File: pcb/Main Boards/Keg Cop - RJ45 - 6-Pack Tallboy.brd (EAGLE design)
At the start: 65 x 51 mm, 17 parts, among them X1 RJ45-8X, X2 RJ45-8X

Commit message: Swap pins, split dirs
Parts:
- moved RELAY 0.40 mm to (13.5, 47.5)
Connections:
- net COOL: now also D32.IO4, RELAY.3; no longer D32.IO0, RELAY.2
- net KDAT: now also D32.IO14; no longer D32.IO27
- net KEG1: now also D32.IO0; no longer D32.IO4
- net SOL: now also D32.IO27, RELAY.2; no longer D32.IO14, RELAY.3
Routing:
- net COOL: track 72.7 -> 91.1 mm
- net KEG1: track 14.9 -> 11.2 mm
- net KDAT: track 25.2 -> 26.1 mm
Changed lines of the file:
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@@
 <wire x1="0" y1="50" x2="0" y2="1" width="0" layer="20"/>
 <wire x1="0" y1="1" x2="1" y2="0" width="0" layer="20" curve="90"/>
-<text x="9.7" y="45.3" size="0.8128" layer="25" align="top-center">G</text>
-<text x="12.3" y="45.3" size="0.8128" layer="25" align="top-center">C</text>
-<text x="14.8" y="45.3" size="0.8128" layer="25" align="top-center">S</text>
-<text x="17.4" y="45.3" size="0.8128" layer="25" align="top-center">V</text>
+<text x="9.7" y="45.7" size="0.8128" layer="25" align="top-center">G</text>
+<text x="14.8" y="45.7" size="0.8128" layer="25" align="top-center">C</text>
+<text x="12.3" y="45.7" size="0.8128" layer="25" align="top-center">S</text>
+<text x="17.4" y="45.7" size="0.8128" layer="25" align="top-center">V</text>
 <text x="9.7" y="39.4" size="0.8128" layer="25" align="top-center">G</text>
 <text x="12.2" y="39.4" size="0.8128" layer="25" align="top-center">V</text>
@@
 <elements>
 <element name="D32" library="Donnie" package="D32_NO_BATT" value="Lolin D32" x="32.5" y="29.27" smashed="yes"/>
-<element name="RELAY" library="Donnie" package="MA04-1" package3d_urn="urn:adsk.eagle:package:8337/1" value="4-PIN" x="13.517" y="47.059975" smashed="yes">
-<attribute name="MF" value="" x="13.517" y="47.059975" size="1.778" layer="27" display="off"/>
-<attribute name="MPN" value="" x="13.517" y="47.059975" size="1.778" layer="27" display="off"/>
-<attribute name="NAME" x="8.437" y="48.710975" size="0.8128" layer="25"/>
-<attribute name="OC_FARNELL" value="unknown" x="13.517" y="47.059975" size="1.778" layer="27" display="off"/>
-<attribute name="OC_NEWARK" value="unknown" x="13.517" y="47.059975" size="1.778" layer="27" display="off"/>
-<attribute name="POPULARITY" value="41" x="13.517" y="47.059975" size="1.778" layer="27" display="off"/>
+<element name="RELAY" library="Donnie" package="MA04-1" package3d_urn="urn:adsk.eagle:package:8337/1" value="4-PIN" x="13.517" y="47.459975" smashed="yes">
+<attribute name="MF" value="" x="13.517" y="47.459975" size="1.778" layer="27" display="off"/>
+<attribute name="MPN" value="" x="13.517" y="47.459975" size="1.778" layer="27" display="off"/>
+<attribute name="NAME" x="8.437" y="49.110975" size="0.8128" layer="25"/>
+<attribute name="OC_FARNELL" value="unknown" x="13.517" y="47.459975" size="1.778" layer="27" display="off"/>
+<attribute name="OC_NEWARK" value="unknown" x="13.517" y="47.459975" size="1.778" layer="27" display="off"/>
+<attribute name="POPULARITY" value="41" x="13.517" y="47.459975" size="1.778" layer="27" display="off"/>
 </element>
 <element name="R1" library="SparkFun-Resistors" library_urn="urn:adsk.eagle:library:532" package="AXIAL-0.3" package3d_urn="urn:adsk.eagle:package:39658/1" value="2.2kΩ" x="28.55335" y="36.8892" smashed="yes" rot="R180">
@@
 <contactref element="C2" pad="1"/>
 <wire x1="22.61" y1="49.59" x2="21.07" y2="49.59" width="1.016" layer="1"/>
-<wire x1="17.327" y1="47.059975" x2="17.327" y2="48.927" width="1.016" layer="1"/>
-<wire x1="17.327" y1="48.927" x2="18" y2="49.6" width="1.016" layer="1"/>
-<wire x1="18" y1="49.6" x2="21.16585" y2="49.6" width="1.016" layer="1"/>
+<wire x1="17.327" y1="47.459975" x2="17.327" y2="49.127" width="1.016" layer="1"/>
+<wire x1="17.327" y1="49.127" x2="17.8" y2="49.6" width="1.016" layer="1"/>
+<wire x1="17.8" y1="49.6" x2="21.16585" y2="49.6" width="1.016" layer="1"/>
 <wire x1="21.16585" y1="49.6" x2="21.07" y2="49.59" width="1.016" layer="1"/>
 <wire x1="32.36335" y1="26.7322" x2="32.36335" y2="29.27145" width="1.016" layer="1"/>
@@
 <contactref element="C3" pad="2"/>
 <contactref element="X1" pad="7"/>
-<wire x1="9.707" y1="41.2" x2="9.707" y2="47.059975" width="1.016" layer="1"/>
+<wire x1="9.707" y1="41.2" x2="9.707" y2="47.459975" width="1.016" layer="1"/>
 <wire x1="35.15785" y1="45.698" x2="35.15785" y2="48.497" width="1.016" layer="1"/>
 <wire x1="35.15785" y1="48.497" x2="35.16285" y2="48.502" width="1.016" layer="1"/>
@@
 </signal>
 <signal name="SOL">
-<contactref element="RELAY" pad="3"/>
-<contactref element="D32" pad="IO14"/>
-<wire x1="21.07" y1="24.19" x2="19.31" y2="24.19" width="1.016" layer="16"/>
-<wire x1="18.7" y1="40.6" x2="14.787" y2="44.513" width="1.016" layer="16"/>
-<wire x1="14.787" y1="44.513" x2="14.787" y2="47.059975" width="1.016" layer="16"/>
-<wire x1="19.31" y1="24.19" x2="18.7" y2="24.8" width="1.016" layer="16"/>
-<wire x1="18.7" y1="24.8" x2="18.7" y2="40.6" width="1.016" layer="16"/>
+<contactref element="RELAY" pad="2"/>
+<wire x1="14.2" y1="45.1" x2="18.7" y2="40.6" width="1.016" layer="16"/>
+<wire x1="14.2" y1="45.1" x2="12.8" y2="45.1" width="1.016" layer="16"/>
+<wire x1="12.8" y1="45.1" x2="12.247" y2="45.653" width="1.016" layer="16"/>
+<wire x1="12.247" y1="45.653" x2="12.247" y2="47.459975" width="1.016" layer="16"/>
+<contactref element="D32" pad="IO27"/>
+<wire x1="18.7" y1="40.6" x2="18.7" y2="27.6" width="1.016" layer="16"/>
+<wire x1="18.7" y1="27.6" x2="19.57" y2="26.73" width="1.016" layer="16"/>
+<wire x1="19.57" y1="26.73" x2="21.07" y2="26.73" width="1.016" layer="16"/>
 </signal>
 <signal name="COOL">
-<contactref element="RELAY" pad="2"/>
-<contactref element="D32" pad="IO0"/>
-<wire x1="25.41" y1="19.11" x2="43.93" y2="19.11" width="1.016" layer="16"/>
 <wire x1="23.2" y1="10.2" x2="22.6" y2="9.6" width="1.016" layer="16"/>
 <wire x1="22.6" y1="9.6" x2="19.6" y2="9.6" width="1.016" layer="16"/>
 <wire x1="18.75555625" y1="10.44444375" x2="19.6" y2="9.6" width="1.016" layer="16"/>
-<wire x1="12.247" y1="47.059975" x2="12.247" y2="45.053" width="1.016" layer="16"/>
 <wire x1="15.6" y1="21.6" x2="18.75555625" y2="18.44444375" width="1.016" layer="16"/>
 <wire x1="18.75555625" y1="18.44444375" x2="18.75555625" y2="10.44444375" width="1.016" layer="16"/>
-<wire x1="12.247" y1="45.053" x2="15.6" y2="41.7" width="1.016" layer="16"/>
-<wire x1="15.6" y1="41.7" x2="15.6" y2="21.6" width="1.016" layer="16"/>
+<wire x1="15.6" y1="21.6" x2="15.6" y2="41.7" width="1.016" layer="16"/>
 <wire x1="23.2" y1="10.2" x2="23.2" y2="16.9" width="1.016" layer="16"/>
 <wire x1="23.2" y1="16.9" x2="25.41" y2="19.11" width="1.016" layer="16"/>
+<contactref element="RELAY" pad="3"/>
+<wire x1="15.6" y1="41.7" x2="13.6" y2="43.7" width="1.016" layer="16"/>
+<wire x1="8.2" y1="43.7" x2="6.8" y2="45.1" width="1.016" layer="16"/>
+<wire x1="6.8" y1="45.1" x2="6.8" y2="48.3" width="1.016" layer="16"/>
+<wire x1="14.787" y1="49.213" x2="14.787" y2="47.459975" width="1.016" layer="16"/>
+<wire x1="13.6" y1="43.7" x2="8.2" y2="43.7" width="1.016" layer="16"/>
+<wire x1="6.8" y1="48.3" x2="8.4" y2="49.9" width="1.016" layer="16"/>
+<wire x1="8.4" y1="49.9" x2="14.1" y2="49.9" width="1.016" layer="16"/>
+<wire x1="14.1" y1="49.9" x2="14.787" y2="49.213" width="1.016" layer="16"/>
+<contactref element="D32" pad="IO4"/>
+<wire x1="25.41" y1="19.11" x2="27.95" y2="21.65" width="1.016" layer="16"/>
+<wire x1="27.95" y1="21.65" x2="43.93" y2="21.65" width="1.016" layer="16"/>
 </signal>
 <signal name="RDAT">
@@
 <signal name="KDAT">
 <contactref element="R5" pad="P$2"/>
-<contactref element="D32" pad="IO27"/>
 <contactref element="X1" pad="5"/>
 <contactref element="X1" pad="6"/>
@@
 <wire x1="10.635" y1="13.12" x2="11.905" y2="14.39" width="1.016" layer="1"/>
 <wire x1="11.905" y1="14.39" x2="11.905" y2="21.505" width="1.016" layer="1"/>
-<wire x1="17.13" y1="26.73" x2="21.07" y2="26.73" width="1.016" layer="1"/>
-<wire x1="11.905" y1="21.505" x2="17.13" y2="26.73" width="1.016" layer="1"/>
-<wire x1="24.74335" y1="26.7322" x2="21.17805" y2="26.7322" width="1.016" layer="1"/>
-<wire x1="21.17805" y1="26.7322" x2="21.07" y2="26.73" width="1.016" layer="1"/>
+<contactref element="D32" pad="IO14"/>
+<wire x1="11.905" y1="21.505" x2="14.59" y2="24.19" width="1.016" layer="1"/>
+<wire x1="14.59" y1="24.19" x2="21.07" y2="24.19" width="1.016" layer="1"/>
+<wire x1="21.07" y1="24.19" x2="23.69" y2="24.19" width="1.016" layer="1"/>
+<wire x1="24.74335" y1="25.24335" x2="24.74335" y2="26.7322" width="1.016" layer="1"/>
+<wire x1="23.69" y1="24.19" x2="24.74335" y2="25.24335" width="1.016" layer="1"/>
 </signal>
 <signal name="KEG4">
@@
 </signal>
 <signal name="KEG1">
-<contactref element="D32" pad="IO4"/>
 <contactref element="X2" pad="1"/>
-<wire x1="49.2" y1="20.4" x2="47.95" y2="21.65" width="1.016" layer="1"/>
-<wire x1="47.95" y1="21.65" x2="43.93" y2="21.65" width="1.016" layer="1"/>
 <wire x1="50.555" y1="11.85" x2="49.2" y2="13.205" width="1.016" layer="1"/>
-<wire x1="49.2" y1="13.205" x2="49.2" y2="20.4" width="1.016" layer="1"/>
+<contactref element="D32" pad="IO0"/>
+<wire x1="49.2" y1="13.205" x2="47.3" y2="15.105" width="1.016" layer="1"/>
+<wire x1="47.3" y1="15.105" x2="47.3" y2="17.8" width="1.016" layer="1"/>
+<wire x1="45.99" y1="19.11" x2="43.93" y2="19.11" width="1.016" layer="1"/>
+<wire x1="47.3" y1="17.8" x2="45.99" y2="19.11" width="1.016" layer="1"/>
 </signal>
 <signal name="KEG2">

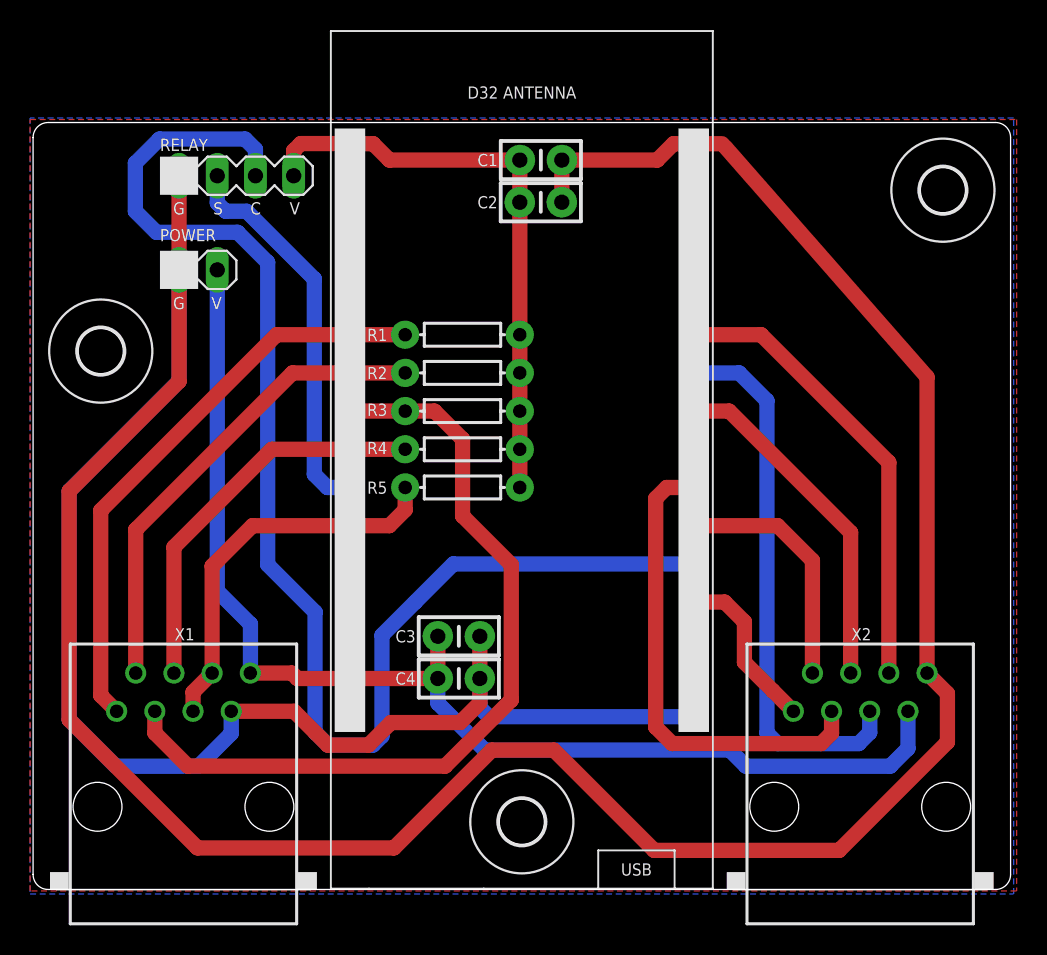
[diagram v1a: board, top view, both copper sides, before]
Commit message: Renamed files
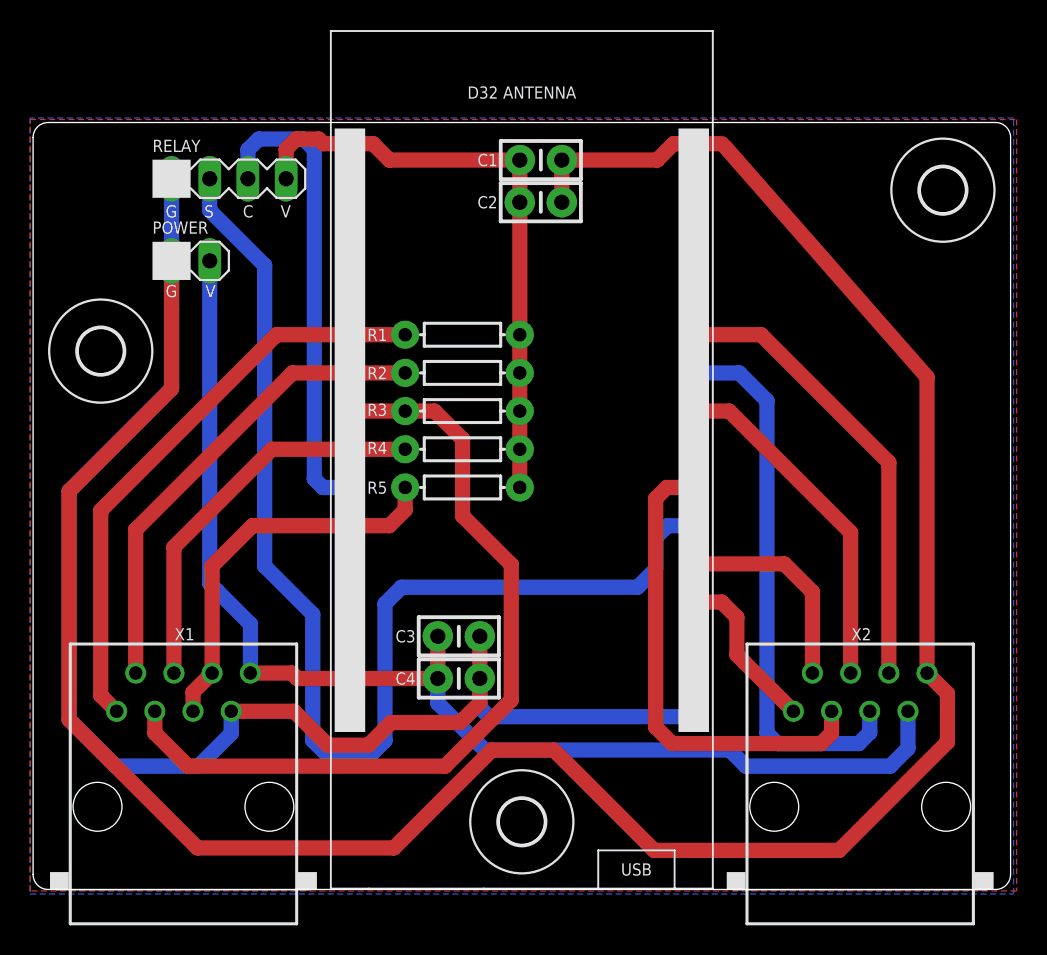
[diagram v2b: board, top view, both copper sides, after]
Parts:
- moved POWER 0.78 mm to (9.21, 41.8)
- moved RELAY 0.54 mm to (13.0, 47.3)
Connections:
- net COOL: now also D32.IO27; no longer D32.IO4
- net KEG2: now also D32.IO4; no longer D32.IO16
- net SOL: now also D32.IO16; no longer D32.IO27
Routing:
- net COOL: track 91.1 -> 31.4 mm
- net SOL: track 26.1 -> 78.7 mm
- net KEG2: track 16.3 -> 14.1 mm
- net 3V3: track 39.3 -> 40.1 mm
- net 5V: track 80.8 -> 81.6 mm
